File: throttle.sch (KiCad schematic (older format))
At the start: 2 parts

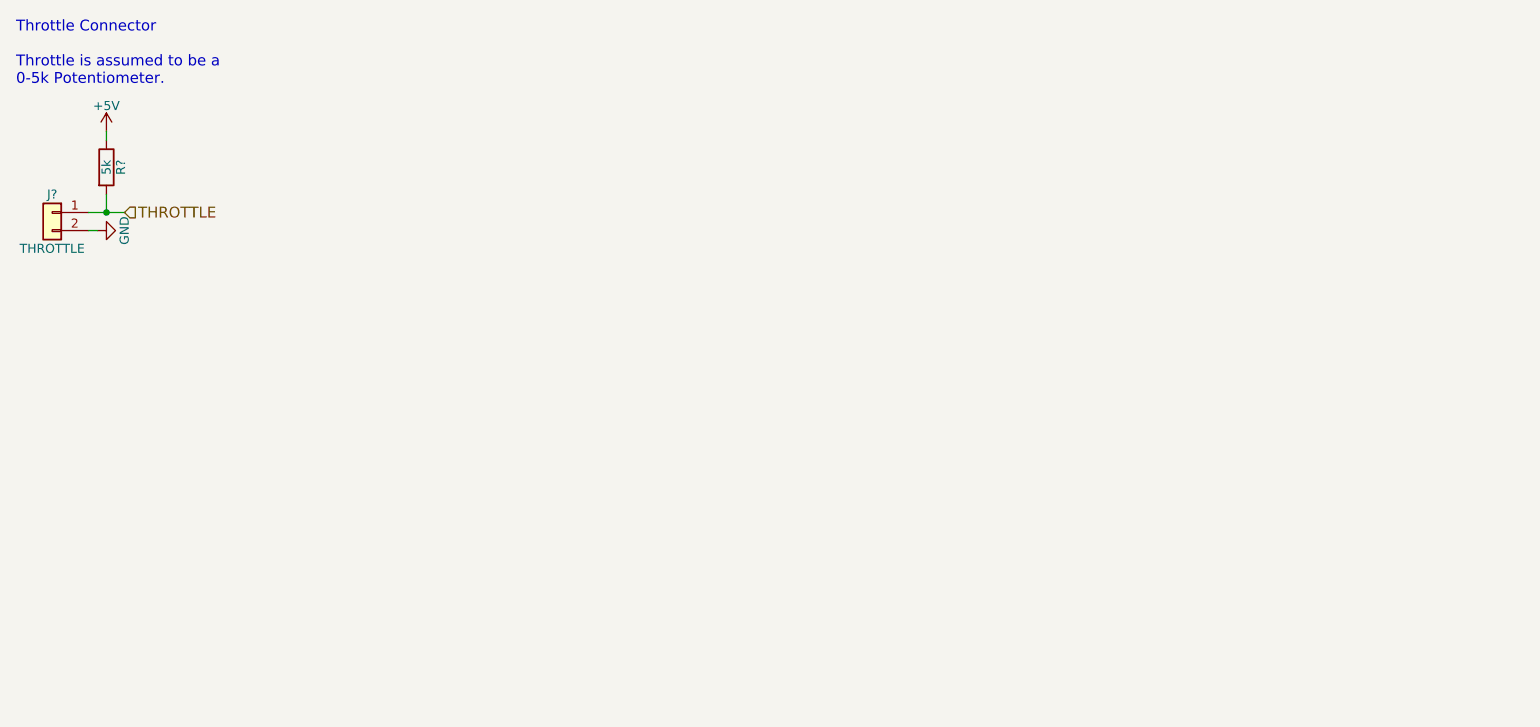
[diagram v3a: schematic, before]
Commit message: Adjust throttle voltage divider.
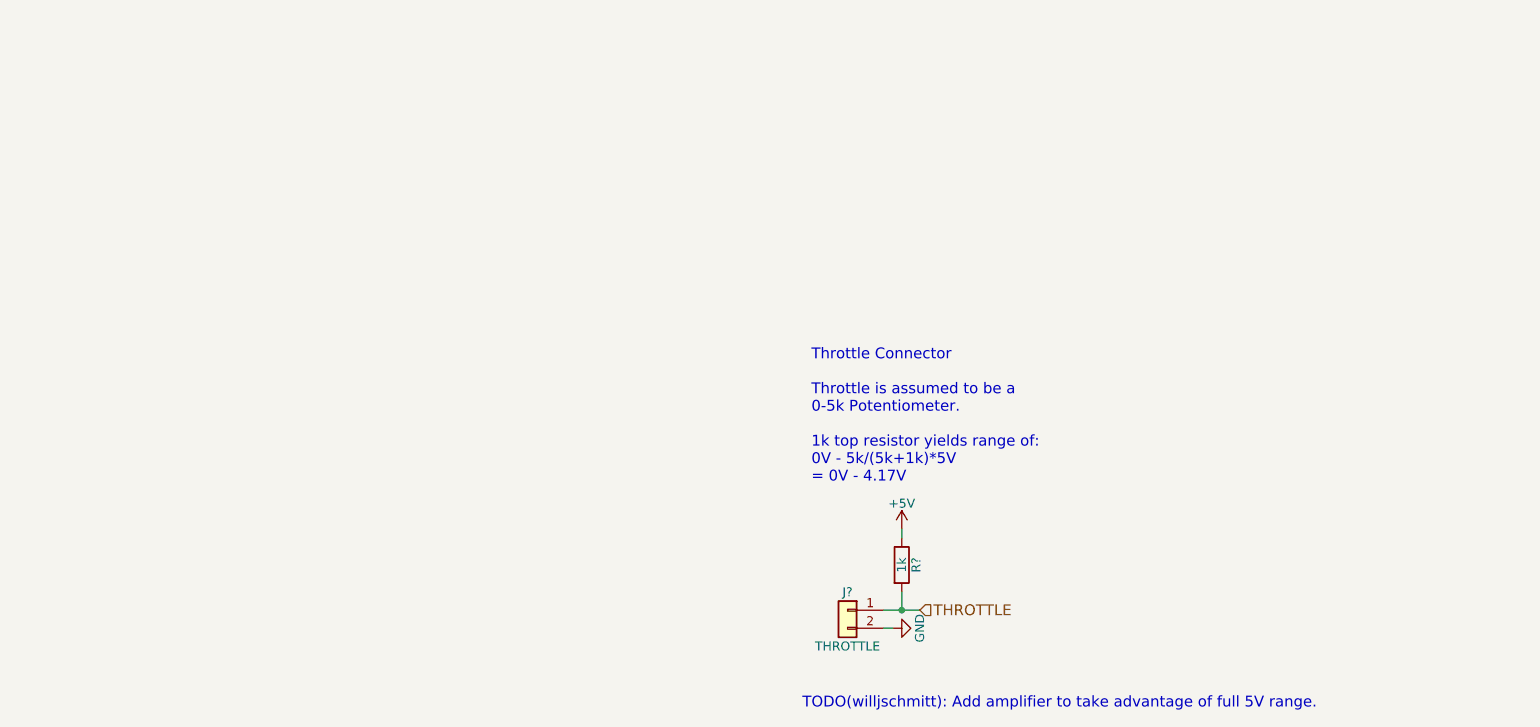
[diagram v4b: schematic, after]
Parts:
- R?: value 5k -> 1k
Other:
- note added: "TODO(willjschmitt): Add amplifier to take advantage of full 5V range."
- note added: "Throttle Connector\n\nThrottle is assumed to be a \n0-5k Potentiometer.\n\n1k top resistor yields range of:\n0V - 5k/(5k+1k)*5V\n= 0V - 4.17V"
- note removed: "Throttle Connector\n\nThrottle is assumed to be a \n0-5k Potentiometer."
- moved on the sheet: J?, R?
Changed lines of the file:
@@
 L Conn_01x02 J?
 U 1 1 5AEE02AA
-P 1100 1850
-F 0 "J?" H 1100 1950 50  0000 C CNN
-F 1 "THROTTLE" H 1100 1650 50  0000 C CNN
-F 2 "" H 1100 1850 50  0001 C CNN
-F 3 "" H 1100 1850 50  0001 C CNN
-	1    1100 1850
+P 5500 4050
+F 0 "J?" H 5500 4150 50  0000 C CNN
+F 1 "THROTTLE" H 5500 3850 50  0000 C CNN
+F 2 "" H 5500 4050 50  0001 C CNN
+F 3 "" H 5500 4050 50  0001 C CNN
+	1    5500 4050
 	-1   0    0    -1
 $EndComp
@@
 L GND #PWR035
 U 1 1 5AEE02B1
-P 1350 1950
-F 0 "#PWR035" H 1350 1700 50  0001 C CNN
-F 1 "GND" H 1350 1800 50  0000 C CNN
-F 2 "" H 1350 1950 50  0001 C CNN
-F 3 "" H 1350 1950 50  0001 C CNN
-	1    1350 1950
+P 5750 4150
+F 0 "#PWR035" H 5750 3900 50  0001 C CNN
+F 1 "GND" H 5750 4000 50  0000 C CNN
+F 2 "" H 5750 4150 50  0001 C CNN
+F 3 "" H 5750 4150 50  0001 C CNN
+	1    5750 4150
 	0    -1   -1   0
 $EndComp
@@
 L R R?
 U 1 1 5AEE02B7
-P 1400 1600
-F 0 "R?" V 1480 1600 50  0000 C CNN
-F 1 "5k" V 1400 1600 50  0000 C CNN
-F 2 "" V 1330 1600 50  0001 C CNN
-F 3 "" H 1400 1600 50  0001 C CNN
-	1    1400 1600
+P 5800 3800
+F 0 "R?" V 5880 3800 50  0000 C CNN
+F 1 "1k" V 5800 3800 50  0000 C CNN
+F 2 "" V 5730 3800 50  0001 C CNN
+F 3 "" H 5800 3800 50  0001 C CNN
+	1    5800 3800
 	1    0    0    -1
 $EndComp
@@
 L +5V #PWR036
 U 1 1 5AEE02BE
-P 1400 1400
-F 0 "#PWR036" H 1400 1250 50  0001 C CNN
-F 1 "+5V" H 1400 1540 50  0000 C CNN
-F 2 "" H 1400 1400 50  0001 C CNN
-F 3 "" H 1400 1400 50  0001 C CNN
-	1    1400 1400
+P 5800 3600
+F 0 "#PWR036" H 5800 3450 50  0001 C CNN
+F 1 "+5V" H 5800 3740 50  0000 C CNN
+F 2 "" H 5800 3600 50  0001 C CNN
+F 3 "" H 5800 3600 50  0001 C CNN
+	1    5800 3600
 	1    0    0    -1
 $EndComp
 Wire Wire Line
-	1350 1950 1300 1950
+	5750 4150 5700 4150
 Wire Wire Line
-	1300 1850 1500 1850
+	5700 4050 5900 4050
 Wire Wire Line
-	1400 1750 1400 1850
-Connection ~ 1400 1850
+	5800 3950 5800 4050
+Connection ~ 5800 4050
 Wire Wire Line
-	1400 1450 1400 1400
-Text Notes 900  1150 0    60   ~ 0
-Throttle Connector\n\nThrottle is assumed to be a \n0-5k Potentiometer.
-Text HLabel 1500 1850 2    60   Input ~ 0
+	5800 3650 5800 3600
+Text Notes 5300 3350 0    60   ~ 0
+Throttle Connector\n\nThrottle is assumed to be a \n0-5k Potentiometer.\n\n1k top resistor yields range of:\n0V - 5k/(5k+1k)*5V\n= 0V - 4.17V
+Text HLabel 5900 4050 2    60   Input ~ 0
 THROTTLE
+Text Notes 5250 4600 0    60   ~ 0
+TODO(willjschmitt): Add amplifier to take advantage of full 5V range.
 $EndSCHEMATC

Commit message: Annotate and add negative IOC faults.
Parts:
- gave numbers to parts that had none: 2
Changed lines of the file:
@@
 $EndDescr
 $Comp
-L Conn_01x02 J?
+L Conn_01x02 J8
 U 1 1 5AEE02AA
 P 5500 4050
-F 0 "J?" H 5500 4150 50  0000 C CNN
+F 0 "J8" H 5500 4150 50  0000 C CNN
 F 1 "THROTTLE" H 5500 3850 50  0000 C CNN
 F 2 "" H 5500 4050 50  0001 C CNN
@@
 $EndComp
 $Comp
-L GND #PWR035
+L GND #PWR36
 U 1 1 5AEE02B1
 P 5750 4150
-F 0 "#PWR035" H 5750 3900 50  0001 C CNN
+F 0 "#PWR36" H 5750 3900 50  0001 C CNN
 F 1 "GND" H 5750 4000 50  0000 C CNN
 F 2 "" H 5750 4150 50  0001 C CNN
@@
 $EndComp
 $Comp
-L R R?
+L R R8
 U 1 1 5AEE02B7
 P 5800 3800
-F 0 "R?" V 5880 3800 50  0000 C CNN
+F 0 "R8" V 5880 3800 50  0000 C CNN
 F 1 "1k" V 5800 3800 50  0000 C CNN
 F 2 "" V 5730 3800 50  0001 C CNN
@@
 $EndComp
 $Comp
-L +5V #PWR036
+L +5V #PWR37
 U 1 1 5AEE02BE
 P 5800 3600
-F 0 "#PWR036" H 5800 3450 50  0001 C CNN
+F 0 "#PWR37" H 5800 3450 50  0001 C CNN
 F 1 "+5V" H 5800 3740 50  0000 C CNN
 F 2 "" H 5800 3600 50  0001 C CNN
